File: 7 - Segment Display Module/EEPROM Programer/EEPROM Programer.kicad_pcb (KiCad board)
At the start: 2 copper layers, 77 x 60 mm, 10 parts, among them J1 Conn_01x02_Pin, U1 Pico, U3 AT28C64B

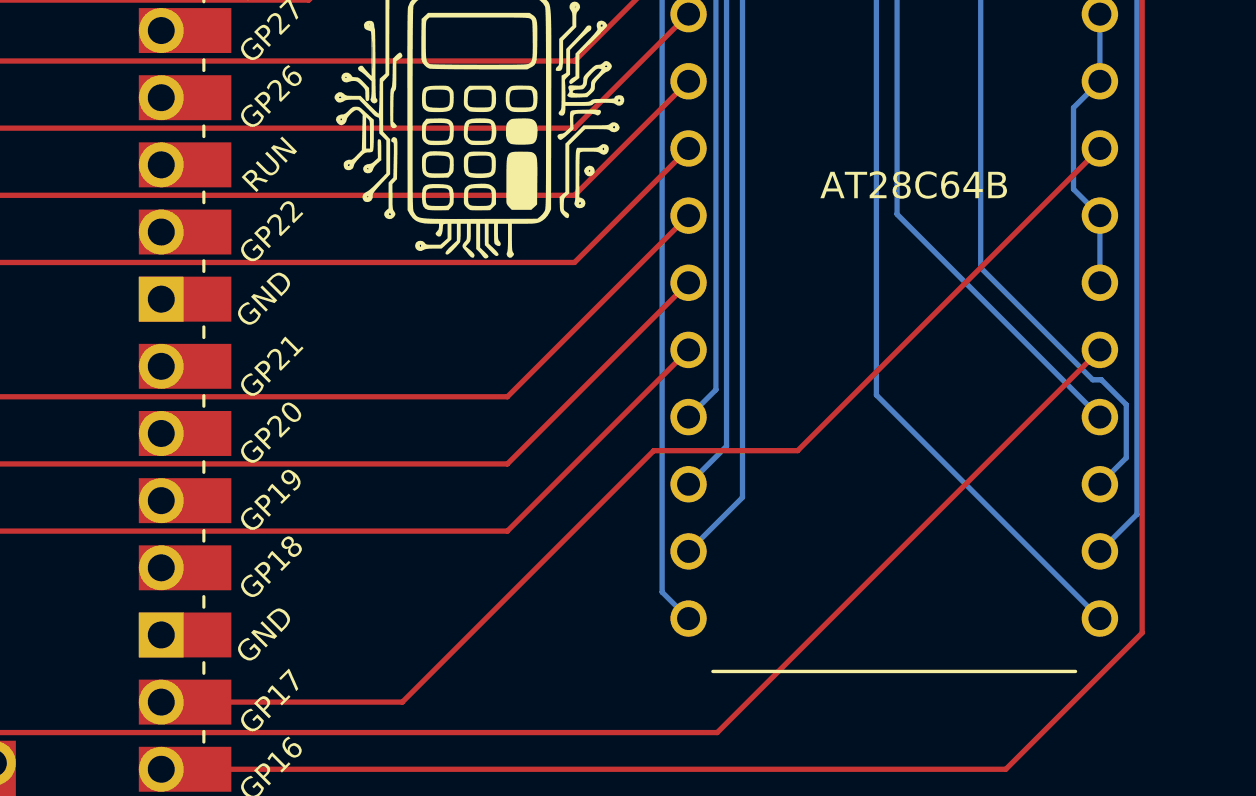
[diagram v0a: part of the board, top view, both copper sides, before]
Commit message: Added a common ground with the pico and the EEPROM
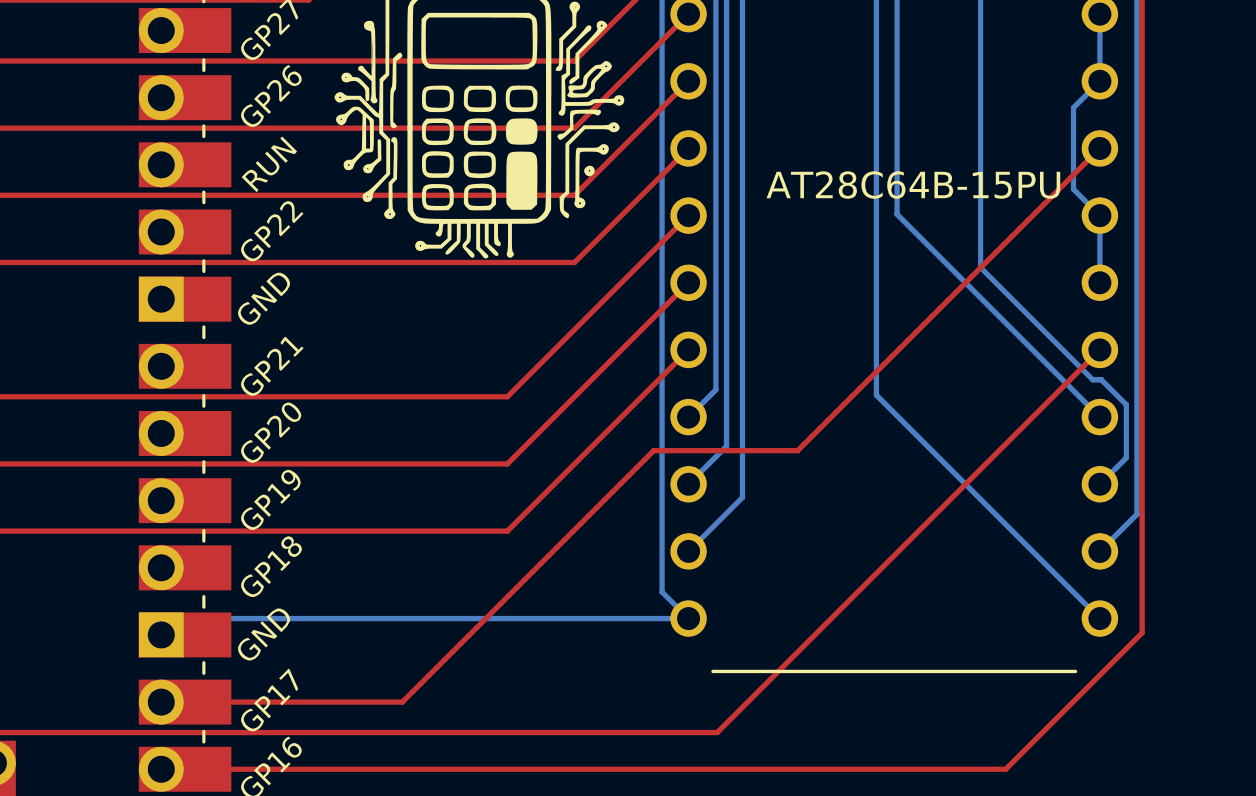
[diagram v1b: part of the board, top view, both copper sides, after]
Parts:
- U3: value AT28C64B -> AT28C64B-15PU
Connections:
- U1 pad 23: unconnected-(U1-GND-Pad23) -> GND
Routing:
- net GND: track 74.6 -> 94.8 mm
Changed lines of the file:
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@@
 	(net 43 "unconnected-(U1-GPIO18-Pad24)")
 	(net 44 "unconnected-(U1-GPIO27_ADC1-Pad32)")
-	(net 45 "unconnected-(U1-GND-Pad23)")
 	(footprint "AT28C64B-15PU:DIP1555W45P254L3733H482Q28"
 		(layer "F.Cu")
@@
 			)
 		)
-		(property "Value" "AT28C64B"
+		(property "Value" "AT28C64B-15PU"
 			(at 0.7787 0.15 0)
 			(layer "F.SilkS")
@@
 			(layers "*.Cu" "*.Mask")
 			(remove_unused_layers no)
-			(net 45 "unconnected-(U1-GND-Pad23)")
+			(net 1 "GND")
 			(pinfunction "GND")
 			(pintype "power_in")
@@
 			)
 			(layers "F.Cu" "F.Mask")
-			(net 45 "unconnected-(U1-GND-Pad23)")
+			(net 1 "GND")
 			(pinfunction "GND")
 			(pintype "power_in")
@@
 	)
 	(segment
+		(start 87.44255 71.86)
+		(end 68.12 71.86)
+		(width 0.2)
+		(layer "B.Cu")
+		(net 1)
+	)
+	(segment
 		(start 103.0001 56.62)
 		(end 103.0001 59.16)
@@
 		(width 0.2)
 		(layer "B.Cu")
+		(net 1)
+	)
+	(segment
+		(start 68.12 71.86)
+		(end 67.5 72.48)
+		(width 0.2)
+		(layer "B.Cu")
